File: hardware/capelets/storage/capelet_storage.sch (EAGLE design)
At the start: 4 parts

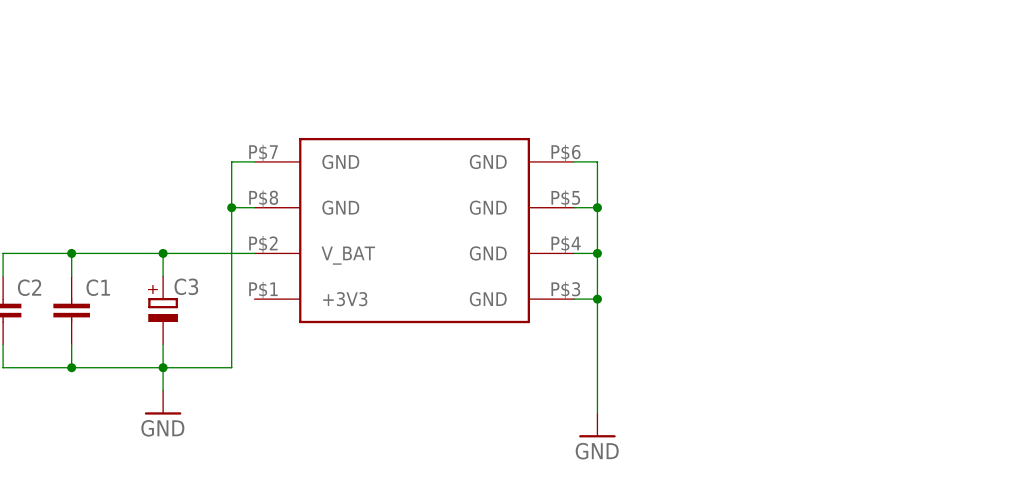
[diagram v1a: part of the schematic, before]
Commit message: hardware: prepared capelets for external manufacturing
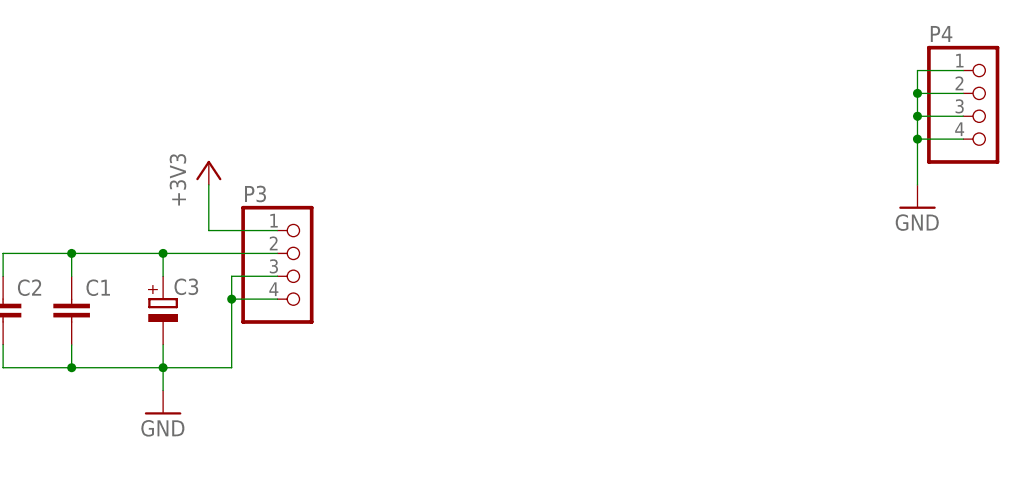
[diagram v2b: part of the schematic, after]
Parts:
- removed U$1: SHPRD_CPLT_S, shepherd:SHPRD_CPLT_S
- added P3, P4: (no value), pinhead:PINHD-1X4
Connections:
- new net +3V3: P3.1
- net GND: now also P3.3, P3.4, P4.1, P4.2, P4.3, P4.4; no longer U$1.GND@1, U$1.GND@2, U$1.GND@3, U$1.GND@4, U$1.GND@5, U$1.GND@6
- net N$1: now also P3.2; no longer U$1.V_BAT
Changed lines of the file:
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@@
 <?xml version="1.0" encoding="utf-8"?>
 <!DOCTYPE eagle SYSTEM "eagle.dtd">
-<eagle version="9.4.2">
+<eagle version="9.5.2">
 <drawing>
 <settings>
@@
 </classes>
 <parts>
-<part name="U$1" library="shepherd" deviceset="SHPRD_CPLT_S" device=""/>
 <part name="C1" library="shepherd" deviceset="C_SMD" device="0805" package3d_urn="urn:adsk.eagle:package:4930364/1"/>
 <part name="C2" library="shepherd" deviceset="C_SMD" device="1210" package3d_urn="urn:adsk.eagle:package:4926069/1"/>
 <part name="C3" library="rcl" library_urn="urn:adsk.eagle:library:334" deviceset="CPOL-EU" device="E5-8.5" package3d_urn="urn:adsk.eagle:package:23374/1"/>
 <part name="GND1" library="supply1" library_urn="urn:adsk.eagle:library:371" deviceset="GND" device=""/>
-<part name="GND2" library="supply1" library_urn="urn:adsk.eagle:library:371" deviceset="GND" device=""/>
 <part name="FRAME1" library="frames" library_urn="urn:adsk.eagle:library:229" deviceset="A4L-LOC" device=""/>
+<part name="P4" library="pinhead" library_urn="urn:adsk.eagle:library:325" deviceset="PINHD-1X4" device="" package3d_urn="urn:adsk.eagle:package:22407/2"/>
+<part name="P3" library="pinhead" library_urn="urn:adsk.eagle:library:325" deviceset="PINHD-1X4" device="" package3d_urn="urn:adsk.eagle:package:22407/2"/>
+<part name="GND3" library="supply1" library_urn="urn:adsk.eagle:library:371" deviceset="GND" device=""/>
+<part name="+3V1" library="supply1" library_urn="urn:adsk.eagle:library:371" deviceset="+3V3" device=""/>
 </parts>
 <sheets>
@@
 </plain>
 <instances>
-<instance part="U$1" gate="G$1" x="71.12" y="53.34" smashed="yes"/>
 <instance part="C1" gate="G$1" x="50.8" y="58.42" smashed="yes">
 <attribute name="NAME" x="52.324" y="58.801" size="1.778" layer="95"/>
@@
 <instance part="GND1" gate="1" x="60.96" y="45.72" smashed="yes">
 <attribute name="VALUE" x="58.42" y="43.18" size="1.778" layer="96"/>
-</instance>
-<instance part="GND2" gate="1" x="109.22" y="43.18" smashed="yes">
-<attribute name="VALUE" x="106.68" y="40.64" size="1.778" layer="96"/>
 </instance>
 <instance part="FRAME1" gate="G$1" x="0" y="0" smashed="yes">
@@
 <attribute name="LAST_DATE_TIME" x="217.17" y="10.16" size="2.286" layer="94"/>
 <attribute name="SHEET" x="230.505" y="5.08" size="2.54" layer="94"/>
+</instance>
+<instance part="P4" gate="A" x="152.4" y="78.74" smashed="yes">
+<attribute name="NAME" x="146.05" y="86.995" size="1.778" layer="95"/>
+<attribute name="VALUE" x="146.05" y="71.12" size="1.778" layer="96"/>
+</instance>
+<instance part="P3" gate="A" x="76.2" y="60.96" smashed="yes">
+<attribute name="NAME" x="69.85" y="69.215" size="1.778" layer="95"/>
+<attribute name="VALUE" x="69.85" y="53.34" size="1.778" layer="96"/>
+</instance>
+<instance part="GND3" gate="1" x="144.78" y="68.58" smashed="yes">
+<attribute name="VALUE" x="142.24" y="66.04" size="1.778" layer="96"/>
+</instance>
+<instance part="+3V1" gate="G$1" x="66.04" y="73.66" smashed="yes">
+<attribute name="VALUE" x="63.5" y="68.58" size="1.778" layer="96" rot="R90"/>
 </instance>
 </instances>
@@
 <segment>
 <pinref part="C2" gate="G$1" pin="1"/>
-<pinref part="U$1" gate="G$1" pin="V_BAT"/>
 <wire x1="43.18" y1="60.96" x2="43.18" y2="63.5" width="0.1524" layer="91"/>
 <wire x1="43.18" y1="63.5" x2="50.8" y2="63.5" width="0.1524" layer="91"/>
 <pinref part="C1" gate="G$1" pin="1"/>
 <wire x1="50.8" y1="63.5" x2="60.96" y2="63.5" width="0.1524" layer="91"/>
-<wire x1="60.96" y1="63.5" x2="71.12" y2="63.5" width="0.1524" layer="91"/>
 <wire x1="50.8" y1="60.96" x2="50.8" y2="63.5" width="0.1524" layer="91"/>
 <junction x="50.8" y="63.5"/>
 <pinref part="C3" gate="G$1" pin="+"/>
 <wire x1="60.96" y1="60.96" x2="60.96" y2="63.5" width="0.1524" layer="91"/>
+<pinref part="P3" gate="A" pin="2"/>
+<wire x1="60.96" y1="63.5" x2="73.66" y2="63.5" width="0.1524" layer="91"/>
 <junction x="60.96" y="63.5"/>
 </segment>
@@
 <net name="GND" class="0">
 <segment>
+<pinref part="C3" gate="G$1" pin="-"/>
 <pinref part="GND1" gate="1" pin="GND"/>
-<pinref part="C3" gate="G$1" pin="-"/>
 <wire x1="60.96" y1="48.26" x2="60.96" y2="50.8" width="0.1524" layer="91"/>
+<wire x1="60.96" y1="50.8" x2="60.96" y2="53.34" width="0.1524" layer="91"/>
+<junction x="60.96" y="50.8"/>
 <pinref part="C1" gate="G$1" pin="2"/>
-<wire x1="60.96" y1="50.8" x2="60.96" y2="53.34" width="0.1524" layer="91"/>
 <wire x1="50.8" y1="53.34" x2="50.8" y2="50.8" width="0.1524" layer="91"/>
 <wire x1="50.8" y1="50.8" x2="60.96" y2="50.8" width="0.1524" layer="91"/>
-<junction x="60.96" y="50.8"/>
+<junction x="50.8" y="50.8"/>
 <pinref part="C2" gate="G$1" pin="2"/>
 <wire x1="43.18" y1="53.34" x2="43.18" y2="50.8" width="0.1524" layer="91"/>
 <wire x1="43.18" y1="50.8" x2="50.8" y2="50.8" width="0.1524" layer="91"/>
-<junction x="50.8" y="50.8"/>
-<wire x1="60.96" y1="50.8" x2="68.58" y2="50.8" width="0.1524" layer="91"/>
-<wire x1="68.58" y1="50.8" x2="68.58" y2="68.58" width="0.1524" layer="91"/>
-<pinref part="U$1" gate="G$1" pin="GND@1"/>
-<wire x1="68.58" y1="68.58" x2="71.12" y2="68.58" width="0.1524" layer="91"/>
-<pinref part="U$1" gate="G$1" pin="GND@2"/>
-<wire x1="68.58" y1="68.58" x2="68.58" y2="73.66" width="0.1524" layer="91"/>
-<wire x1="68.58" y1="73.66" x2="71.12" y2="73.66" width="0.1524" layer="91"/>
-<junction x="68.58" y="68.58"/>
-</segment>
-<segment>
-<pinref part="GND2" gate="1" pin="GND"/>
-<pinref part="U$1" gate="G$1" pin="GND@3"/>
-<wire x1="109.22" y1="45.72" x2="109.22" y2="58.42" width="0.1524" layer="91"/>
-<wire x1="109.22" y1="58.42" x2="109.22" y2="63.5" width="0.1524" layer="91"/>
-<wire x1="109.22" y1="63.5" x2="109.22" y2="68.58" width="0.1524" layer="91"/>
-<wire x1="109.22" y1="68.58" x2="109.22" y2="73.66" width="0.1524" layer="91"/>
-<wire x1="109.22" y1="73.66" x2="106.68" y2="73.66" width="0.1524" layer="91"/>
-<pinref part="U$1" gate="G$1" pin="GND@4"/>
-<wire x1="106.68" y1="68.58" x2="109.22" y2="68.58" width="0.1524" layer="91"/>
-<junction x="109.22" y="68.58"/>
-<pinref part="U$1" gate="G$1" pin="GND@5"/>
-<wire x1="106.68" y1="63.5" x2="109.22" y2="63.5" width="0.1524" layer="91"/>
-<junction x="109.22" y="63.5"/>
-<pinref part="U$1" gate="G$1" pin="GND@6"/>
-<wire x1="106.68" y1="58.42" x2="109.22" y2="58.42" width="0.1524" layer="91"/>
-<junction x="109.22" y="58.42"/>
+<pinref part="P3" gate="A" pin="3"/>
+<wire x1="73.66" y1="60.96" x2="68.58" y2="60.96" width="0.1524" layer="91"/>
+<wire x1="68.58" y1="60.96" x2="68.58" y2="58.42" width="0.1524" layer="91"/>
+<wire x1="68.58" y1="58.42" x2="68.58" y2="50.8" width="0.1524" layer="91"/>
+<wire x1="68.58" y1="50.8" x2="60.96" y2="50.8" width="0.1524" layer="91"/>
+<pinref part="P3" gate="A" pin="4"/>
+<wire x1="73.66" y1="58.42" x2="68.58" y2="58.42" width="0.1524" layer="91"/>
+<junction x="68.58" y="58.42"/>
+</segment>
+<segment>
+<pinref part="GND3" gate="1" pin="GND"/>
+<wire x1="144.78" y1="71.12" x2="144.78" y2="76.2" width="0.1524" layer="91"/>
+<pinref part="P4" gate="A" pin="4"/>
+<wire x1="144.78" y1="76.2" x2="149.86" y2="76.2" width="0.1524" layer="91"/>
+<pinref part="P4" gate="A" pin="3"/>
+<wire x1="149.86" y1="78.74" x2="144.78" y2="78.74" width="0.1524" layer="91"/>
+<wire x1="144.78" y1="78.74" x2="144.78" y2="76.2" width="0.1524" layer="91"/>
+<junction x="144.78" y="76.2"/>
+<pinref part="P4" gate="A" pin="2"/>
+<wire x1="149.86" y1="81.28" x2="144.78" y2="81.28" width="0.1524" layer="91"/>
+<wire x1="144.78" y1="81.28" x2="144.78" y2="78.74" width="0.1524" layer="91"/>
+<junction x="144.78" y="78.74"/>
+<pinref part="P4" gate="A" pin="1"/>
+<wire x1="149.86" y1="83.82" x2="144.78" y2="83.82" width="0.1524" layer="91"/>
+<wire x1="144.78" y1="83.82" x2="144.78" y2="81.28" width="0.1524" layer="91"/>
+<junction x="144.78" y="81.28"/>
 </segment>
 </net>
+<net name="+3V3" class="0">
+<segment>
+<pinref part="P3" gate="A" pin="1"/>
+<wire x1="73.66" y1="66.04" x2="66.04" y2="66.04" width="0.1524" layer="91"/>
+<wire x1="66.04" y1="66.04" x2="66.04" y2="71.12" width="0.1524" layer="91"/>
+<pinref part="+3V1" gate="G$1" pin="+3V3"/>
+</segment>
+</net>
